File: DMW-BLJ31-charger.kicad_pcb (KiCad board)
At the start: 2 copper layers, 137 x 147 mm, 24 parts, among them J1 BAT+, J10 gnd, J11 BAT+, J12 BAT-, J13 BAT+, J14 BAT-, J15 BAT+, J16 BAT-, J17 BAT-, J18 BAT+, J19 BAT-, J2 BAT-, J20 BAT+, J3 BAT+, J4 BAT+, J5 gnd, J6 gnd, J7 Vin, J8 Vin, J9 gnd

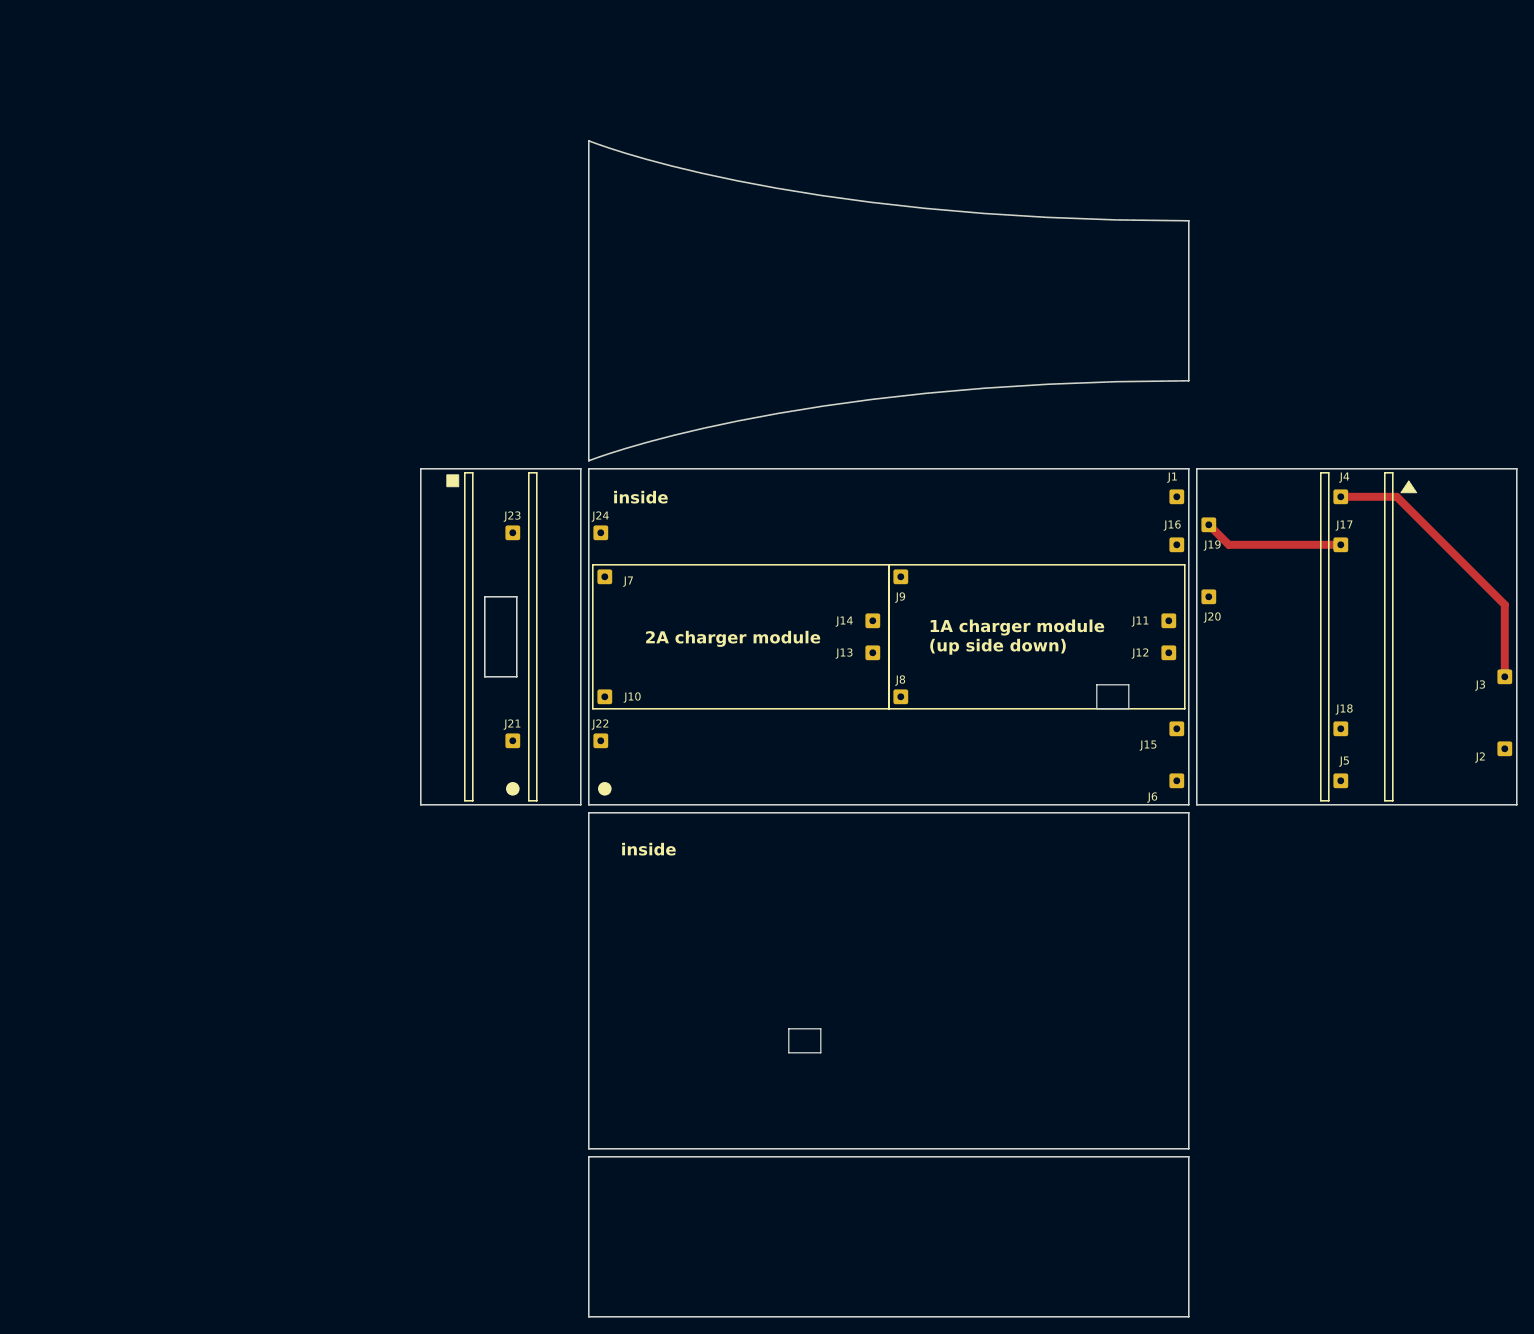
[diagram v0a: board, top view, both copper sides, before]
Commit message: refined case pads
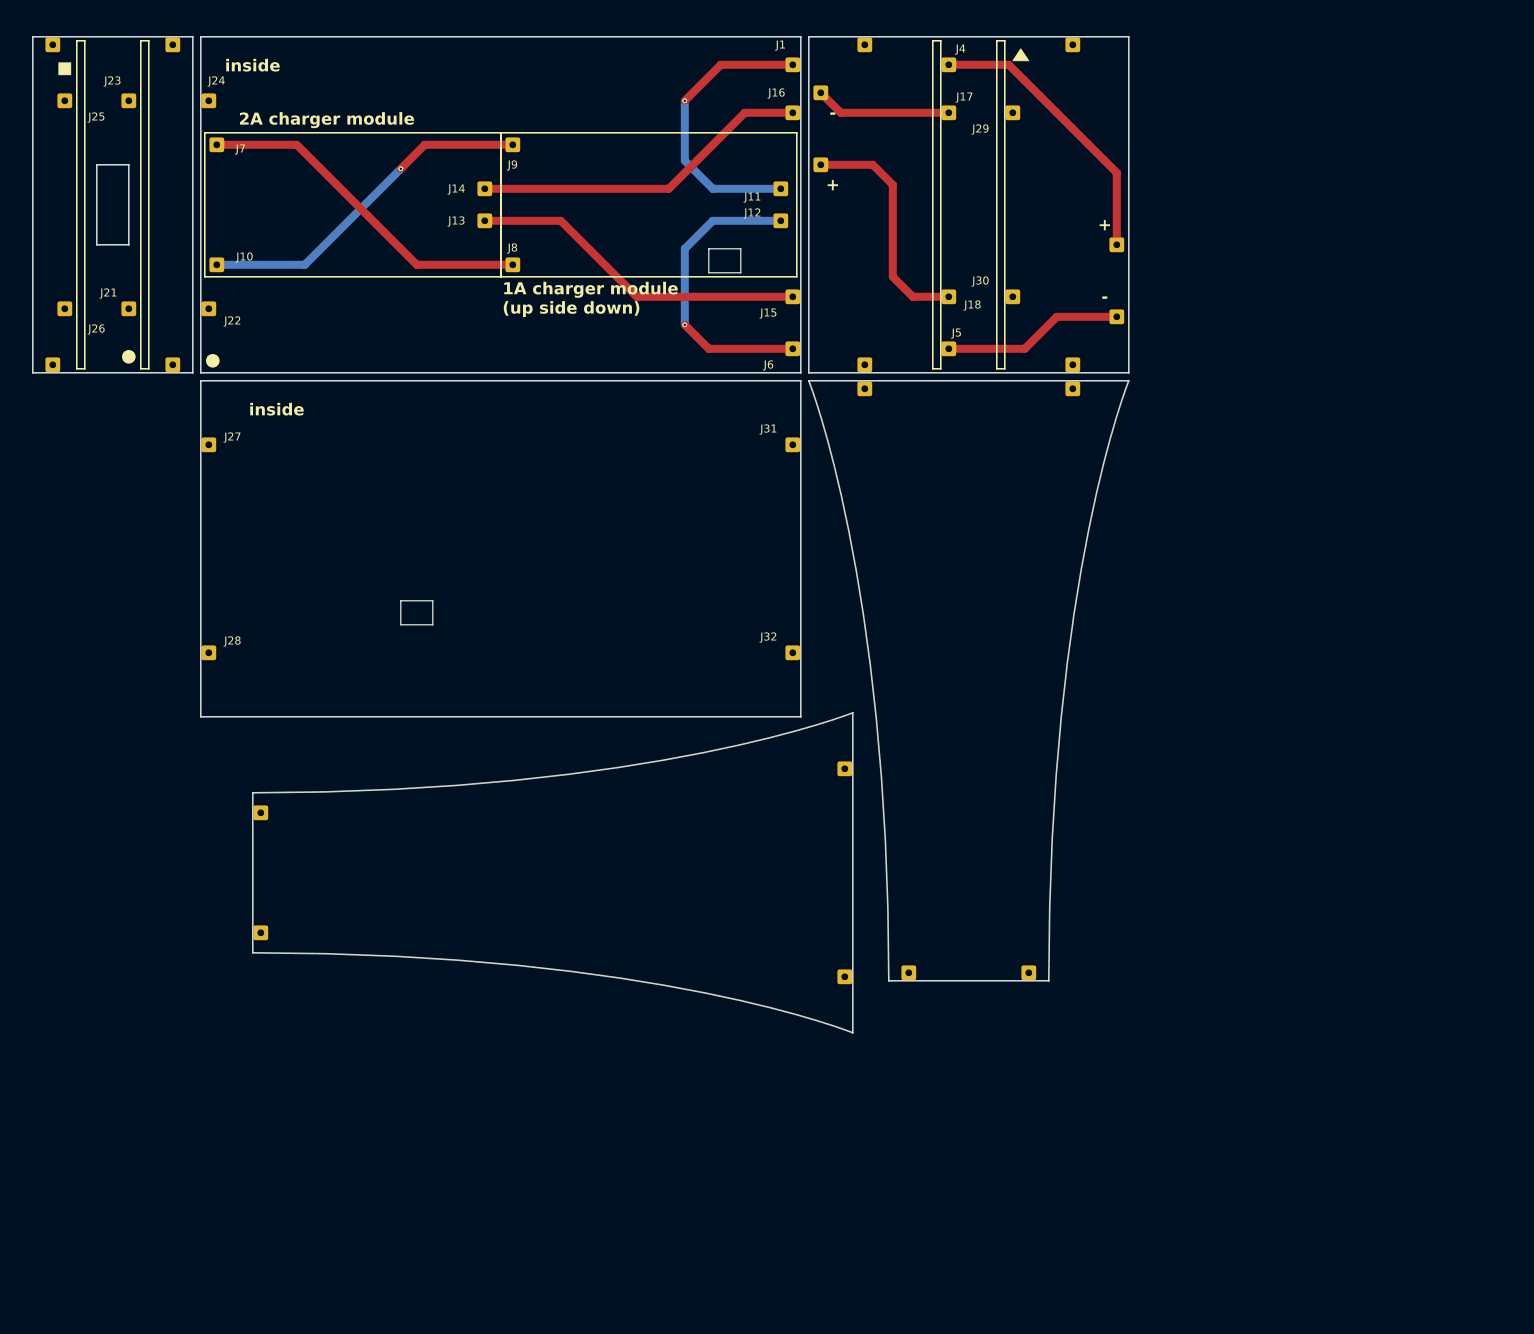
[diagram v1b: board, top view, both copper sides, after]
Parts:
- added J25: ~, Connector_Wire:SolderWire-0.25sqmm_1x01_D0.65mm_OD1.7mm, F.Cu at (31.0, 35.0)
- added J26: ~, Connector_Wire:SolderWire-0.25sqmm_1x01_D0.65mm_OD1.7mm, F.Cu at (31.0, 61.0)
- added J27: ~, Connector_Wire:SolderWire-0.25sqmm_1x01_D0.65mm_OD1.7mm, F.Cu at (49.0, 78.0)
- added J28: ~, Connector_Wire:SolderWire-0.25sqmm_1x01_D0.65mm_OD1.7mm, F.Cu at (49.0, 104.0)
- added J29: ~, Connector_Wire:SolderWire-0.25sqmm_1x01_D0.65mm_OD1.7mm, F.Cu at (149.5, 36.5)
- added J30: ~, Connector_Wire:SolderWire-0.25sqmm_1x01_D0.65mm_OD1.7mm, F.Cu at (149.5, 59.5)
- added J31: ~, Connector_Wire:SolderWire-0.25sqmm_1x01_D0.65mm_OD1.7mm, F.Cu at (122.0, 78.0)
- added J32: ~, Connector_Wire:SolderWire-0.25sqmm_1x01_D0.65mm_OD1.7mm, F.Cu at (122.0, 104.0)
- added J33: ~, Connector_Wire:SolderWire-0.25sqmm_1x01_D0.65mm_OD1.7mm, F.Cu at (128.5, 118.5)
- added J34: ~, Connector_Wire:SolderWire-0.25sqmm_1x01_D0.65mm_OD1.7mm, F.Cu at (128.5, 144.5)
- added J35: ~, Connector_Wire:SolderWire-0.25sqmm_1x01_D0.65mm_OD1.7mm, F.Cu at (151.5, 144.0)
- added J36: ~, Connector_Wire:SolderWire-0.25sqmm_1x01_D0.65mm_OD1.7mm, F.Cu at (136.5, 144.0)
- added J37: ~, Connector_Wire:SolderWire-0.25sqmm_1x01_D0.65mm_OD1.7mm, F.Cu at (131.0, 71.0)
- added J38: ~, Connector_Wire:SolderWire-0.25sqmm_1x01_D0.65mm_OD1.7mm, F.Cu at (157.0, 28.0)
- added J39: ~, Connector_Wire:SolderWire-0.25sqmm_1x01_D0.65mm_OD1.7mm, F.Cu at (157.0, 71.0)
- added J40: ~, Connector_Wire:SolderWire-0.25sqmm_1x01_D0.65mm_OD1.7mm, F.Cu at (131.0, 28.0)
- added J41: ~, Connector_Wire:SolderWire-0.25sqmm_1x01_D0.65mm_OD1.7mm, F.Cu at (157.0, 68.0)
- added J42: ~, Connector_Wire:SolderWire-0.25sqmm_1x01_D0.65mm_OD1.7mm, F.Cu at (131.0, 68.0)
- added J43: ~, Connector_Wire:SolderWire-0.25sqmm_1x01_D0.65mm_OD1.7mm, F.Cu at (29.5, 68.0)
- added J44: ~, Connector_Wire:SolderWire-0.25sqmm_1x01_D0.65mm_OD1.7mm, F.Cu at (44.5, 68.0)
- added J45: ~, Connector_Wire:SolderWire-0.25sqmm_1x01_D0.65mm_OD1.7mm, F.Cu at (29.5, 28.0)
- added J46: ~, Connector_Wire:SolderWire-0.25sqmm_1x01_D0.65mm_OD1.7mm, F.Cu at (44.5, 28.0)
- added J47: ~, Connector_Wire:SolderWire-0.25sqmm_1x01_D0.65mm_OD1.7mm, F.Cu at (55.5, 124.0)
- added J48: ~, Connector_Wire:SolderWire-0.25sqmm_1x01_D0.65mm_OD1.7mm, F.Cu at (55.5, 139.0)
- J19, J2: value BAT- -> -
- J20, J3: value BAT+ -> +
- moved J17 72.9 mm to (141.5, 36.5)
- moved J18 72.9 mm to (141.5, 59.5)
- moved J22 72.9 mm to (49.0, 61.0)
- moved J24 72.9 mm to (49.0, 35.0)
- moved J4 72.9 mm to (141.5, 30.5)
- moved J5 72.9 mm to (141.5, 66.0)
- moved J10 72.6 mm to (50.0, 55.5)
- moved J11 72.6 mm to (120.5, 46.0)
- moved J12 72.6 mm to (120.5, 50.0)
- moved J13 72.6 mm to (83.5, 50.0)
- moved J14 72.6 mm to (83.5, 46.0)
- moved J19 72.6 mm to (125.5, 34.0)
- moved J2 72.6 mm to (162.5, 62.0)
- moved J20 72.6 mm to (125.5, 43.0)
- moved J3 72.6 mm to (162.5, 53.0)
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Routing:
- net Net-(J13-Pin_1): track 0.00 -> 71.5 mm
- net Net-(J12-Pin_1): track 0.00 -> 59.8 mm, vias 0 -> 1
- net Net-(J7-Pin_1): track 0.00 -> 43.2 mm
- net Net-(J10-Pin_1): track 0.00 -> 43.2 mm, vias 0 -> 2
- net Net-(J14-Pin_1): track 17.5 -> 59.5 mm
- net Net-(J1-Pin_1): track 35.1 -> 71.4 mm, vias 0 -> 1
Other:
- board size 137 x 147 mm -> 137 x 124.5 mm
- board text added: "7.2V,1A"
- board text added: "7.2V,2A"
- board text added: "DUAL DMW-BLJ31 CHARGER V1.0"
- board text removed: "7.2V, 1A and 2A"
- board text removed: "DUAL DMW-BLJ31 CHARGER"

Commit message: move charger module to different side
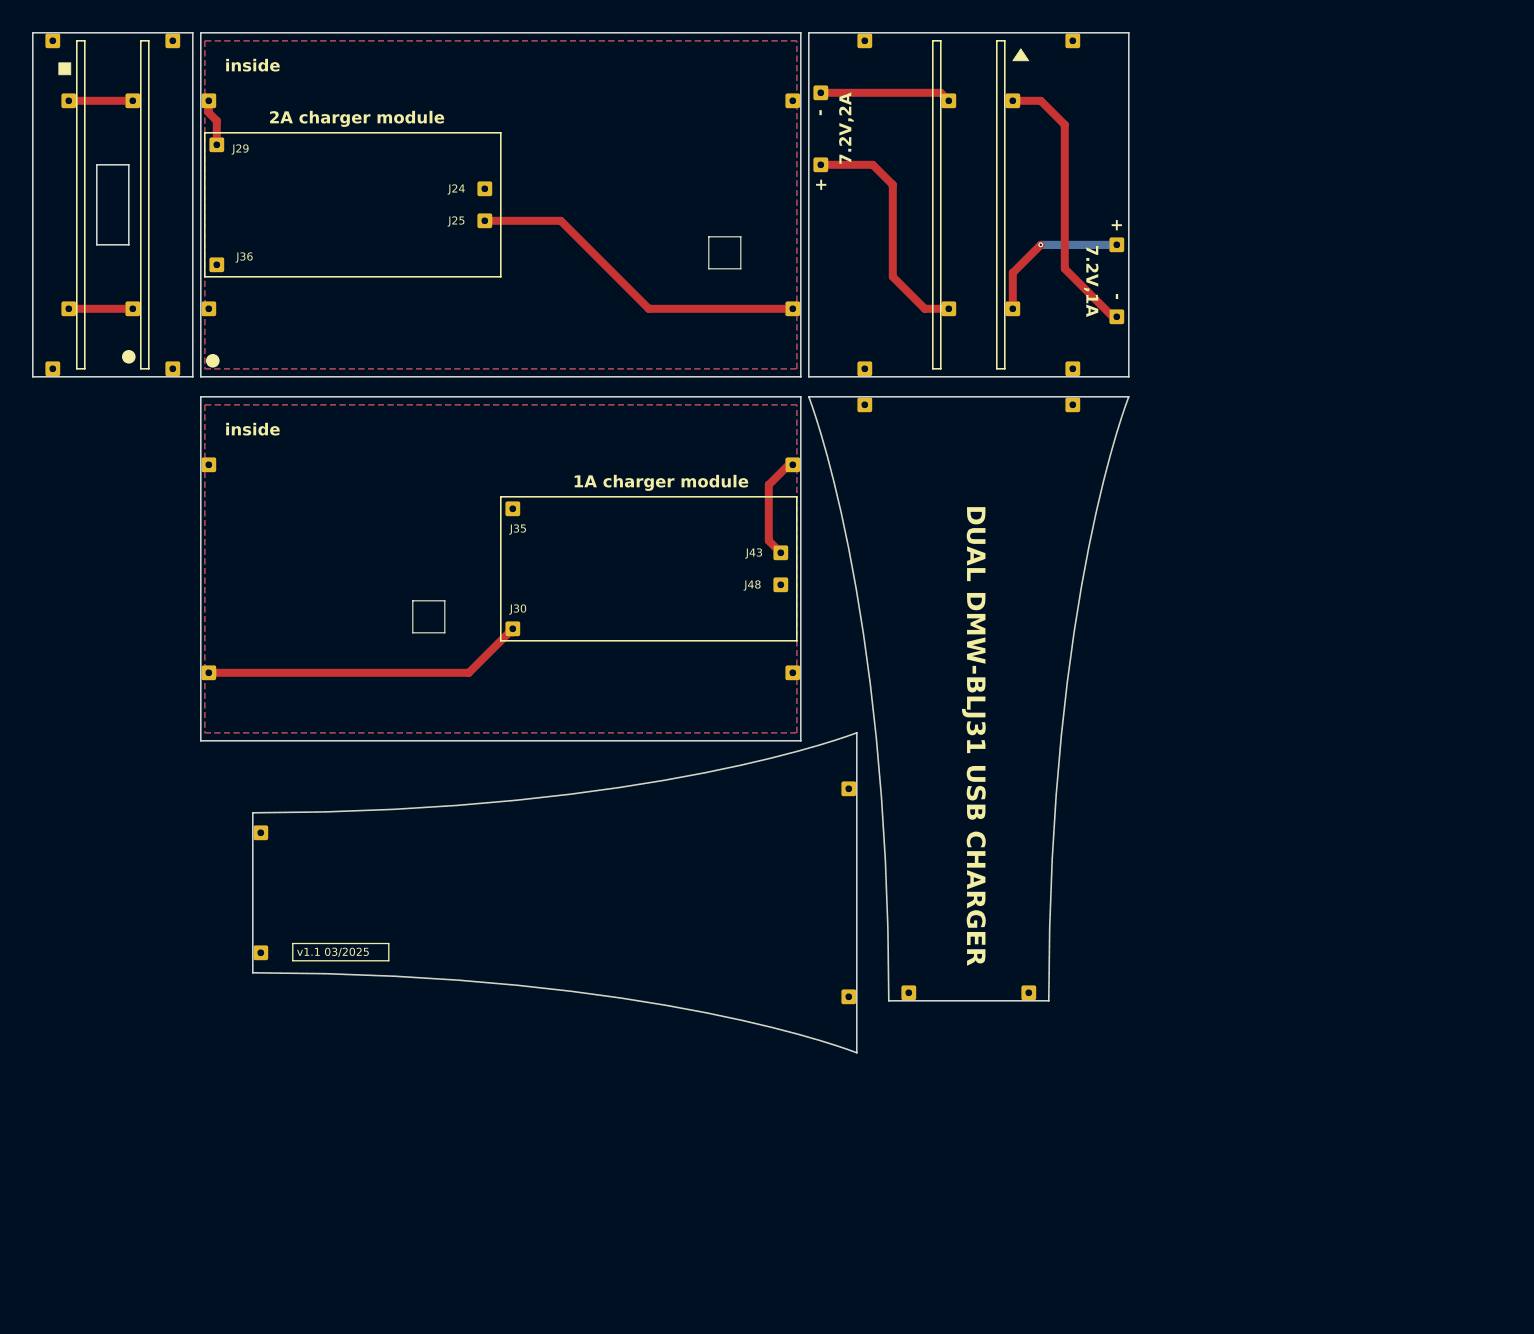
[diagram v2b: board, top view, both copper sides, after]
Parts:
- removed the J12 at (120.5, 50.0)
- removed the J29 at (149.5, 36.5)
- removed the J30 at (149.5, 59.5)
- removed the J31 at (122.0, 78.0)
- removed the J32 at (122.0, 104.0)
- added J48: BAT-, Connector_Wire:SolderWire-0.25sqmm_1x01_D0.65mm_OD1.7mm, F.Cu at (120.5, 95.5)
- moved J42 50.0 mm to (122.0, 80.5)
- moved J30 45.5 mm to (87.0, 101.0)
- moved J35 45.5 mm to (87.0, 86.0)
- moved J43 45.5 mm to (120.5, 91.5)
- moved J37 40.5 mm to (122.0, 106.5)
- moved J47 32.0 mm to (149.5, 35.0)
- moved J45 31.5 mm to (149.5, 61.0)
- moved J5 2.55 mm to (129.0, 121.0)
- moved J6 2.55 mm to (129.0, 147.0)
- moved J19 2.50 mm to (55.5, 126.5)
- moved J20 2.50 mm to (55.5, 141.5)
- moved J32 2.50 mm to (49.0, 106.5)
- moved J41 2.50 mm to (49.0, 80.5)
- moved J7 2.50 mm to (151.5, 146.5)
- moved J8 2.50 mm to (136.5, 146.5)
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- renumbered J38 to J10, J39 to J11, J40 to J12, J41 to J13, J42 to J14, J43 to J15, J44 to J16, J45 to J17, J46 to J18, J47 to J19, J48 to J20, J16 to J21, J17 to J22, J19 to J23, J14 to J24, J13 to J25, J20 to J26, J18 to J27, J15 to J28, J7 to J29, J8 to J30, J25 to J31, J28 to J32, J23 to J33, J24 to J34, J9 to J35, J10 to J36, J6 to J37, J21 to J38, J22 to J39, J26 to J40, J27 to J41, J1 to J42, J11 to J43, J3 to J44, J4 to J45, J2 to J46, J5 to J47, J33 to J5, J34 to J6, J35 to J7, J36 to J8, J37 to J9
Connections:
- J21 pad 1: Net-(J14-Pin_1) -> GND
- J22 pad 1: Net-(J14-Pin_1) -> GND
- J23 pad 1: Net-(J14-Pin_1) -> GND
- J24 pad 1: Net-(J14-Pin_1) -> GND
- J29 pad 1: Net-(J7-Pin_1) -> Net-(J29-Pin_1)
- J30 pad 1: Net-(J7-Pin_1) -> Net-(J29-Pin_1)
- J31 pad 1: unconnected-(J25-Pin_1-Pad1) -> Net-(J29-Pin_1)
- J32 pad 1: unconnected-(J28-Pin_1-Pad1) -> Net-(J29-Pin_1)
- J33 pad 1: unconnected-(J23-Pin_1-Pad1) -> Net-(J29-Pin_1)
- J34 pad 1: unconnected-(J24-Pin_1-Pad1) -> Net-(J29-Pin_1)
- J35 pad 1: Net-(J10-Pin_1) -> GND
- J36 pad 1: Net-(J10-Pin_1) -> GND
- J37 pad 1: Net-(J12-Pin_1) -> GND
- J38 pad 1: unconnected-(J21-Pin_1-Pad1) -> GND
- J39 pad 1: unconnected-(J22-Pin_1-Pad1) -> GND
- J40 pad 1: unconnected-(J26-Pin_1-Pad1) -> GND
- J41 pad 1: unconnected-(J27-Pin_1-Pad1) -> GND
- J46 pad 1: Net-(J12-Pin_1) -> GND
- J47 pad 1: Net-(J12-Pin_1) -> GND
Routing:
- net Net-(J12-Pin_1): track 59.8 -> 0.00 mm, vias 1 -> 0
- net Net-(J14-Pin_1): track 59.5 -> 0.00 mm
- net GND: track 0.00 -> 59.1 mm
- net Net-(J29-Pin_1): track 0.00 -> 54.2 mm
- net Net-(J7-Pin_1): track 43.2 -> 0.00 mm
- net Net-(J10-Pin_1): track 43.2 -> 0.00 mm, vias 2 -> 0
- net Net-(J42-Pin_1): track 71.4 -> 32.4 mm
- net Net-(J25-Pin_1): track 71.5 -> 73.2 mm
- added copper zone on B.Cu, net GND
- added copper zone on F.Cu, net GND
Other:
- board size 137 x 124.5 mm -> 137 x 127.5 mm
- board text added: "1A charger module"
- board text added: "DUAL DMW-BLJ31 USB CHARGER"
- board text added: "v1.1 03/2025"
- board text removed: "1A charger module (up side down)"
- board text removed: "DUAL DMW-BLJ31 CHARGER V1.0"

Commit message: release version 1.2 with better mechanical mount
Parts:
- moved J10 3.50 mm to (160.5, 27.5)
- moved J12 3.50 mm to (134.5, 27.5)
- moved J13 3.50 mm to (160.5, 68.5)
- moved J14 3.50 mm to (134.5, 68.5)
- moved J22 3.50 mm to (145.0, 35.0)
- moved J23 3.50 mm to (129.0, 34.0)
- moved J26 3.50 mm to (129.0, 43.0)
- moved J27 3.50 mm to (145.0, 61.0)
- moved J44 3.50 mm to (166.0, 53.0)
- moved J45 3.50 mm to (153.0, 61.0)
- moved J46 3.50 mm to (166.0, 62.0)
- moved J47 3.50 mm to (153.0, 35.0)
- moved J15 2.00 mm to (27.5, 68.5)
- moved J16 2.00 mm to (42.5, 68.5)
- moved J17 2.00 mm to (27.5, 27.5)
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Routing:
- net GND: track 59.1 -> 68.9 mm, vias 0 -> 125
- net Net-(J42-Pin_1): track 32.4 -> 30.1 mm
- net Net-(J25-Pin_1): track 73.2 -> 72.7 mm
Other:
- board size 137 x 127.5 mm -> 142.5 x 127.5 mm
- board text added: "NOTES FOR MANUFACTURING - Use a PCB thinkness of 1mm - Two layers NOTES FOR ASSEMBLY - vias for mechanical assembly are used for electrical connections - all vias must be soldered - Spring loaded pins compressed max length must be <2.7mm (0.106{dblquote}) For instance: Mill Max 0986-0-15-20-76-14-11-0 Farnell code: 3771554"
- board text added: "v1.2 03/2025"
- board text removed: "v1.1 03/2025"
